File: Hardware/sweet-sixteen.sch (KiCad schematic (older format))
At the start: 81 parts, among them P1 SDA_I, P10 VIN_O, P11 GND_O, P12 SDA_O, P13 CLK_O, P14 LE_O, P15 ~OE_O, P2 CLK_I, P3 LE_I, P4 ~OE_I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

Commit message: remove wrong gnd pin on pi connecor, add some labels
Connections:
- net GND: no longer P5.35 (P35)
- no-connect marks 25 -> 26
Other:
- note added: "GPIO 10"
- note added: "GPIO 11"
- note added: "GPIO 18"
- note added: "GPIO 22"
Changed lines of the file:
@@
-$EndComp
-$Comp
-L GND #PWR011
-U 1 1 584E8B98
-P 4950 13850
-F 0 "#PWR011" H 4950 13600 50  0001 C CNN
-F 1 "GND" H 4950 13700 50  0000 C CNN
-F 2 "" H 4950 13850 50  0000 C CNN
-F 3 "" H 4950 13850 50  0000 C CNN
-	1    4950 13850
-	1    0    0    -1
 $EndComp
 $Comp
@@
 Wire Wire Line
 	8350 1250 8400 1250
-Wire Wire Line
-	4950 13850 4950 13750
 Wire Wire Line
 	3450 13150 3450 13250
@@
 Wire Wire Line
 	17850 5200 7500 5200
+NoConn ~ 4950 13750
+Text Notes 4900 14550 0    60   ~ 0
+GPIO 22
+Text Notes 4900 12800 0    60   ~ 0
+GPIO 18
+Text Notes 4900 14400 0    60   ~ 0
+GPIO 10
+Text Notes 4900 14250 0    60   ~ 0
+GPIO 11
 $EndSCHEMATC

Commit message: clean up BOM, add Button
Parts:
- added SW1: SW_PUSH, ADTSM61:ADTSM61, symbol SW_PUSH
- C1, C2, C3, C30, C4, C5, C6, C7, C8, C9: value 10nf -> 0.1μF
- C31: value 100nf -> 0.1μF
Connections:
- net GND: now also SW1.1
- net at P5.11 (P11): now also SW1.2
- no-connect marks 26 -> 25

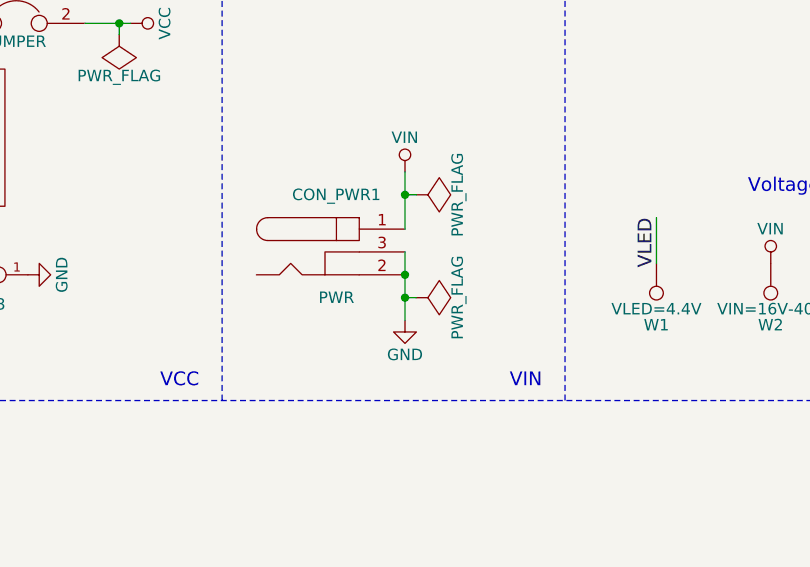
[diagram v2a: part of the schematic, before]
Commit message: place new connector footprint, update gerbers with soldermask
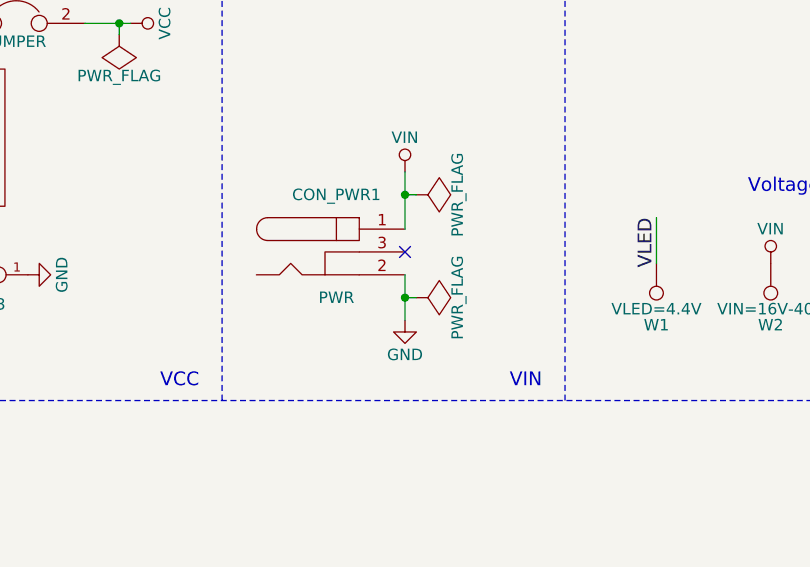
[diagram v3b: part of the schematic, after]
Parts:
- CON_PWR1: footprint Connect:BARREL_JACK -> DELL-PCON:DELL-PCON
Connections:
- net GND: no longer CON_PWR1.3
- no-connect marks 25 -> 26
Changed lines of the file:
@@
 F 0 "CON_PWR1" H 5800 3200 50  0000 C CNN
 F 1 "PWR" H 5800 2750 50  0000 C CNN
-F 2 "Connect:BARREL_JACK" H 5800 2950 50  0001 C CNN
+F 2 "DELL-PCON:DELL-PCON" H 5800 2950 50  0001 C CNN
 F 3 "" H 5800 2950 50  0000 C CNN
 	1    5800 2950
@@
 Wire Wire Line
 	19800 6800 19800 5750
-Wire Wire Line
-	6100 2950 6100 3250
-Connection ~ 6100 3050
 Wire Wire Line
 	1150 1850 1150 1950
@@
 Wire Wire Line
 	2850 14350 2850 14250
+Wire Wire Line
+	6100 3050 6100 3250
+NoConn ~ 6100 2950
 $EndSCHEMATC

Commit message: rev1 changes
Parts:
- removed W5: GND, Measurement_Points:Measurement_Point_Round-SMD-Pad_Big, symbol TEST_1P
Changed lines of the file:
@@
 Wire Notes Line
 	6800 3600 6800 450
-$Comp
-L TEST_1P W5
-U 1 1 58AC03B7
-P 8500 3000
-F 0 "W5" H 8500 3270 50  0000 C CNN
-F 1 "GND" H 8500 3200 50  0000 C CNN
-F 2 "Measurement_Points:Measurement_Point_Round-SMD-Pad_Big" H 8700 3000 50  0001 C CNN
-F 3 "" H 8700 3000 50  0000 C CNN
-	1    8500 3000
-	-1   0    0    1
-$EndComp
-Connection ~ 8700 3000
 Text Label 3550 8850 0    60   ~ 0
 SDA_12
@@
 SDA_9O
 Wire Wire Line
-	8500 3000 8700 3000
-Wire Wire Line
 	18050 5400 18050 7300
